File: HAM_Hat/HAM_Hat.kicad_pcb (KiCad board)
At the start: 2 copper layers, 65 x 56.5 mm, 44 parts, among them J101 TL212V-02P-G12S, J102 DB-9RS-C, J103 NCW254-02S, J104 SMA6252A2, J109 socket, J3 FHDH2.54-40, M101 Fan, Q101 BSS138, Q102 BSS138, T101 SM-LP-5001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

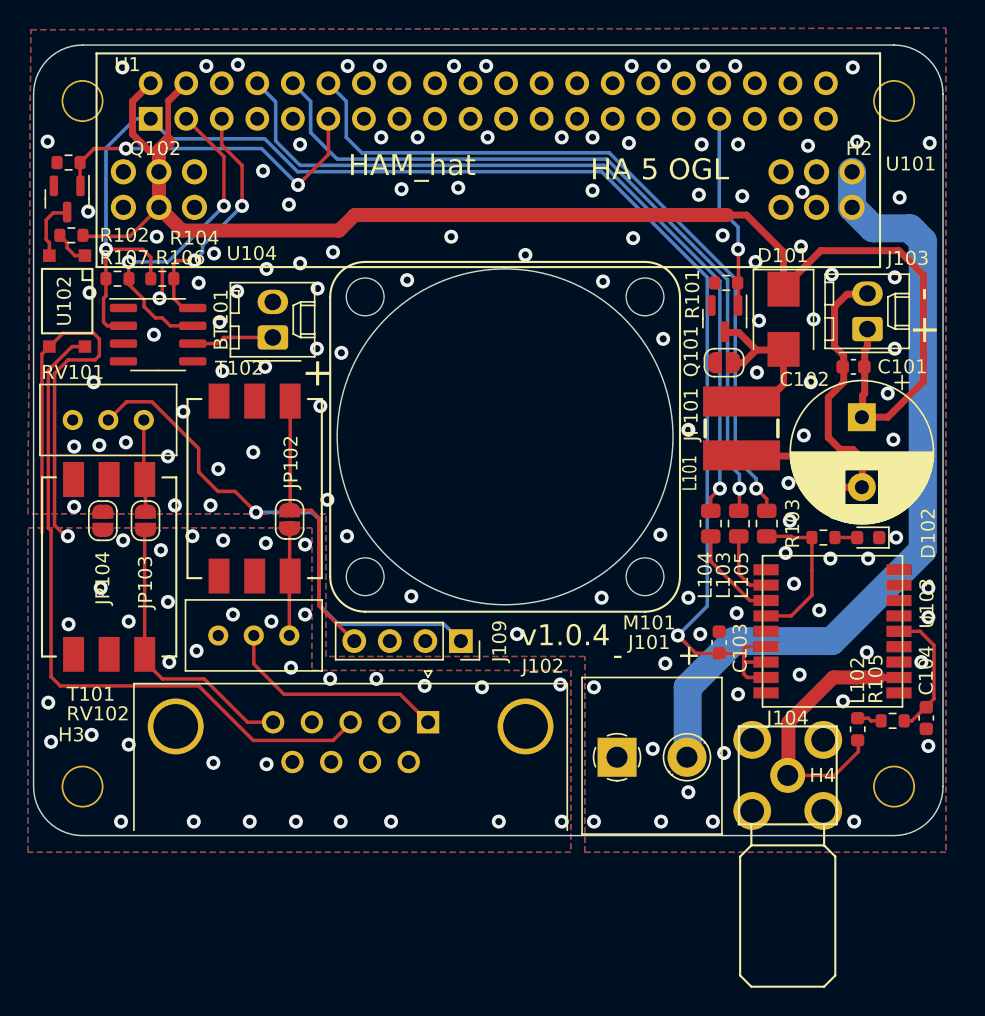
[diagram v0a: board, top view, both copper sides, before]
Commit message: Replace the DB9 connector
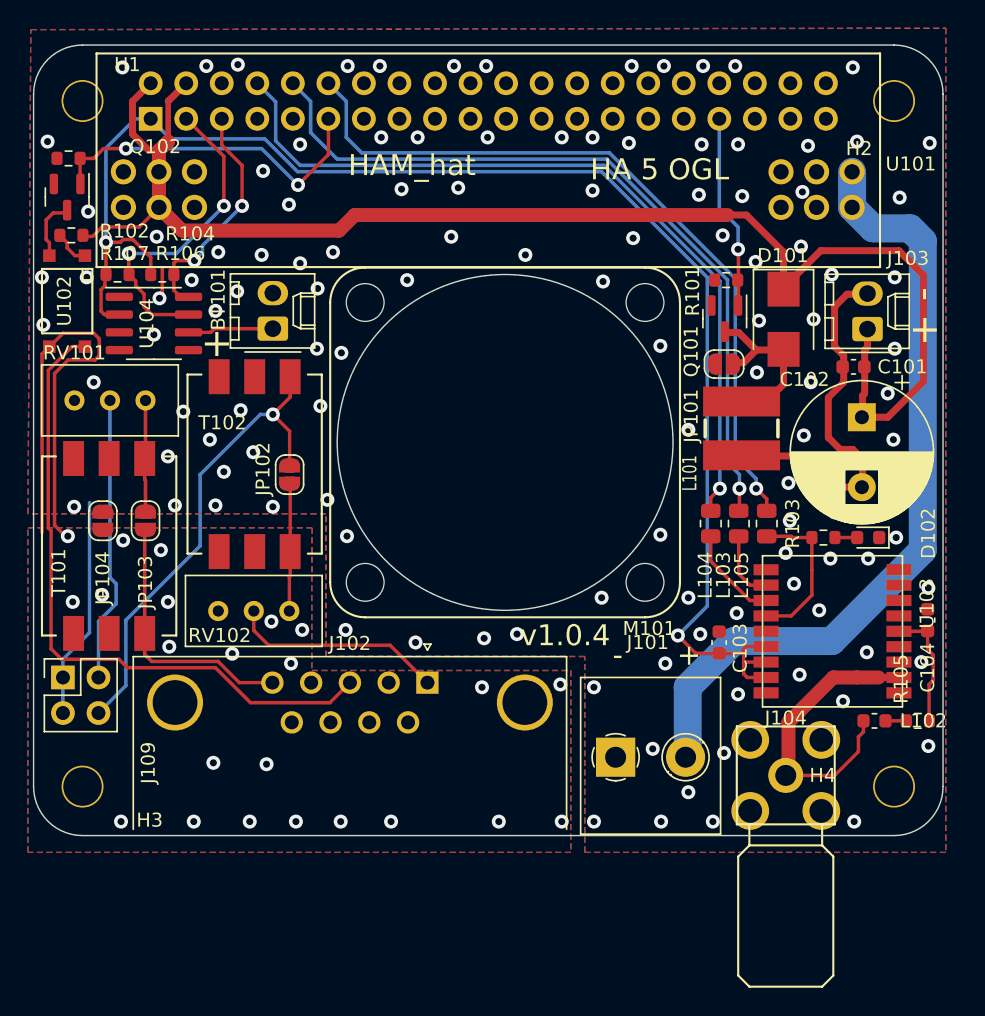
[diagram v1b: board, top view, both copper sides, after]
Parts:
- J102: footprint Connector_Dsub:DSUB-9_Female_Horizontal_P2.77x2.84mm_EdgePinOffset4.94mm_Housed_MountingHolesOffset7.48mm -> Connector_Dsub:DSUB-9_Female_Horizontal_P2.77x2.84mm_EdgePinOffset7.70mm_Housed_MountingHolesOffset9.12mm
- J109: footprint Connector_PinSocket_2.54mm:PinSocket_1x04_P2.54mm_Vertical -> Connector_PinSocket_2.54mm:PinSocket_2x02_P2.54mm_Vertical
- moved J109 28.6 mm to (118.1, 114.7), turned to 90 degrees
- moved C104 7.00 mm to (179.9, 110.6), turned to -90 degrees
- moved JP102 3.20 mm to (134.3, 100.2)
- moved J102 2.83 mm to (144.2, 115.1)
- moved R105 1.80 mm to (179.2, 117.8)
- moved RV102 1.75 mm to (129.2, 110.0)
- moved T102 1.75 mm to (131.8, 99.5)
- moved T101 1.50 mm to (121.4, 105.3)
- moved RV101 1.41 mm to (118.9, 94.9)
- moved L102 1.34 mm to (176.1, 117.8), turned to 180 degrees
- moved U104 0.85 mm to (124.6, 89.4)
- moved BT101 0.63 mm to (133.1, 89.8)
- moved M101 0.40 mm to (149.7, 97.9)
- moved R102 0.30 mm to (118.5, 77.6)
- moved R106 0.30 mm to (125.2, 85.9)
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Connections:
- J109 pad 1: Net-(J109-Pin_1) -> GND
- J109 pad 3: GND -> Net-(J109-Pin_3)
- RV101 pad 2: Net-(J109-Pin_1) -> Net-(J109-Pin_3)
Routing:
- net Net-(J109-Pin_1): track 37.4 -> 0.00 mm, vias 1 -> 0
- net Net-(J109-Pin_3): track 0.00 -> 20.5 mm
- net GND: track 2.32 -> 18.2 mm, vias 120 -> 121
- net Net-(J109-Pin_4): track 20.0 -> 34.4 mm, vias 0 -> 1
- net Net-(J102-Pad3): track 49.2 -> 46.9 mm
- net Net-(JP103-B): track 20.5 -> 18.9 mm
- net Net-(J104-In): track 19.5 -> 21.1 mm
- net Net-(JP102-B): track 7.69 -> 9.14 mm
- net Net-(JP103-A): track 6.60 -> 8.00 mm
- net Net-(J102-Pad1): track 16.2 -> 15.3 mm
- net /SCL: track 17.9 -> 17.2 mm
- net Net-(U103-VCC_RF): track 9.47 -> 8.79 mm
- net GNDA: vias 36 -> 23

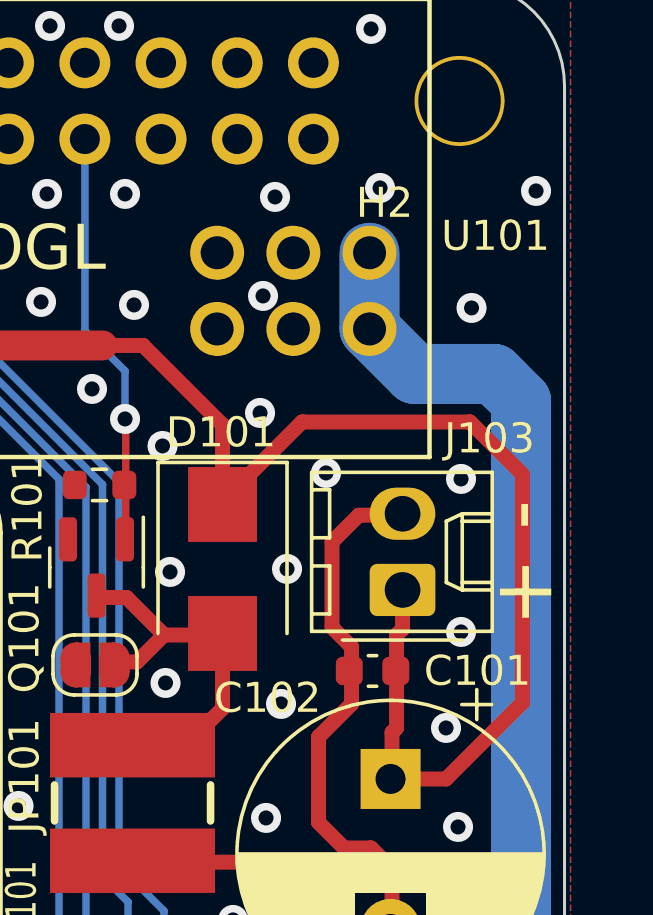
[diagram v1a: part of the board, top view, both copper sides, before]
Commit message: Add CW keying function
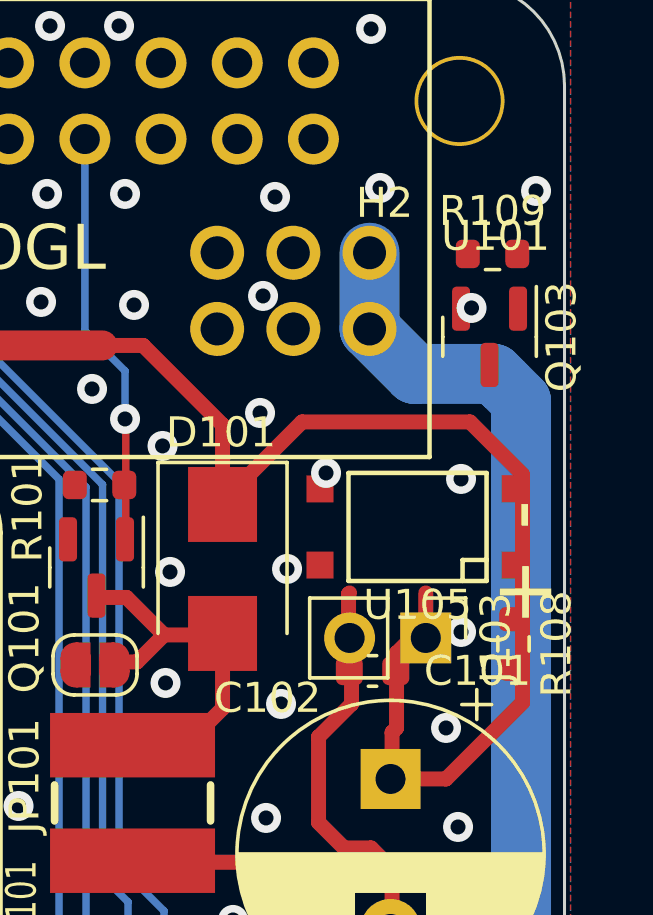
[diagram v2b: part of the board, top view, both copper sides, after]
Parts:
- added Q103: BSS138, Package_TO_SOT_SMD:SOT-23, F.Cu at (178.5, 81.4)
- added R108: 510R, Resistor_SMD:R_0603_1608Metric, F.Cu at (179.3, 91.6)
- added R109: 10k, Resistor_SMD:R_0603_1608Metric, F.Cu at (178.6, 78.6)
- added U105: TLP185, l_optocoupler:11-4M1S, F.Cu at (176.1, 87.7)
- J103: footprint Connector_Molex:Molex_KK-254_AE-6410-02A_1x02_P2.54mm_Vertical -> Connector_PinHeader_2.54mm:PinHeader_1x02_P2.54mm_Vertical
- moved J103 1.78 mm to (176.4, 91.4), turned to -90 degrees
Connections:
- J102 pad 2: unconnected-(J102-Pad2) -> Net-(J102-Pad2)
- J3 pad 40: unconnected-(J3-BCM21-Pad40) -> /CW_KEY
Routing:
- net Net-(J103-Pin_2): track 27.4 -> 22.8 mm
- net GNDA: vias 23 -> 24
- net GND: vias 121 -> 120

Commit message: Some progress on the CW keying support
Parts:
- moved R108 0.10 mm to (179.4, 91.6)
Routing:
- net Net-(J102-Pad2): track 0.00 -> 52.7 mm, vias 0 -> 2
- net GNDA: track 34.7 -> 76.2 mm, vias 24 -> 25
- net /P5V_HAT: track 103.8 -> 98.0 mm
- net Net-(Q103-D): track 0.00 -> 4.48 mm
- net Net-(R108-Pad1): track 0.00 -> 1.83 mm
- net Net-(J103-Pin_2): track 22.8 -> 21.6 mm
- net GND: vias 120 -> 118

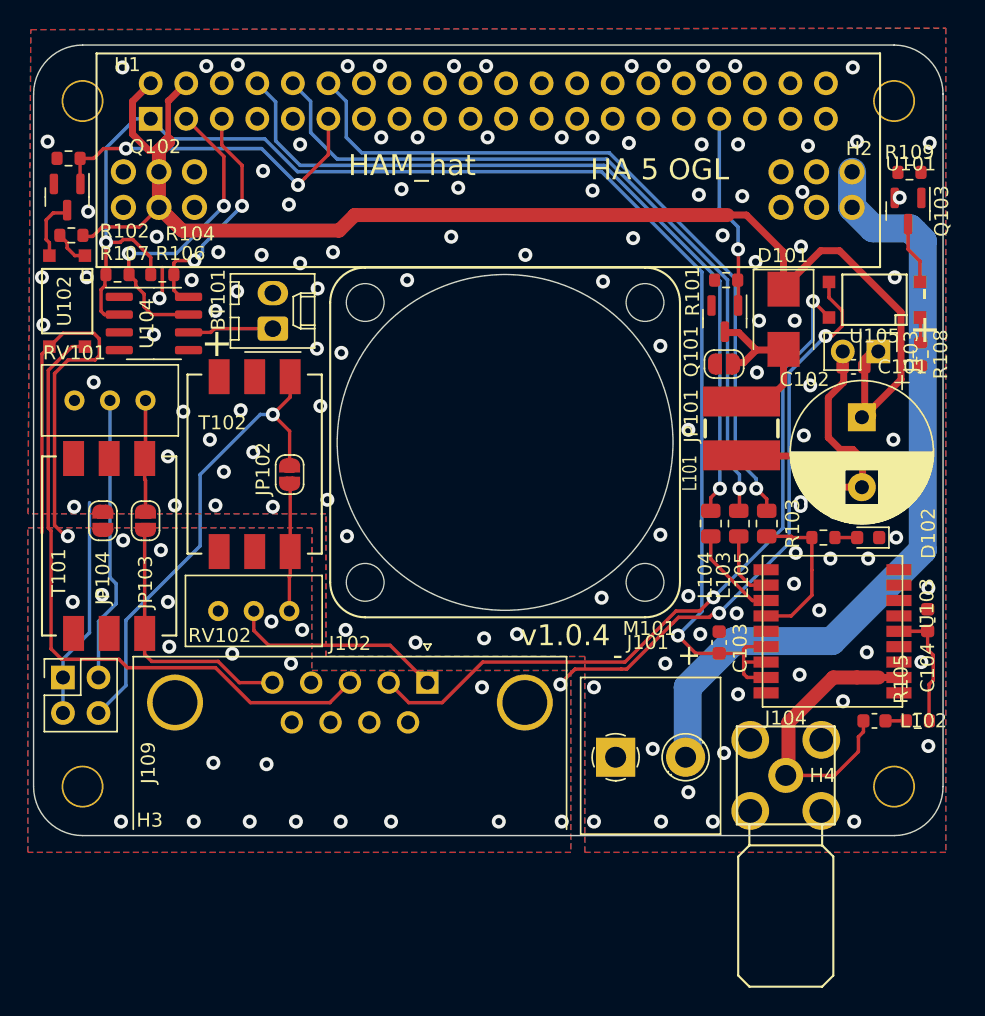
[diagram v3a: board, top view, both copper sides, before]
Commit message: CW keying added
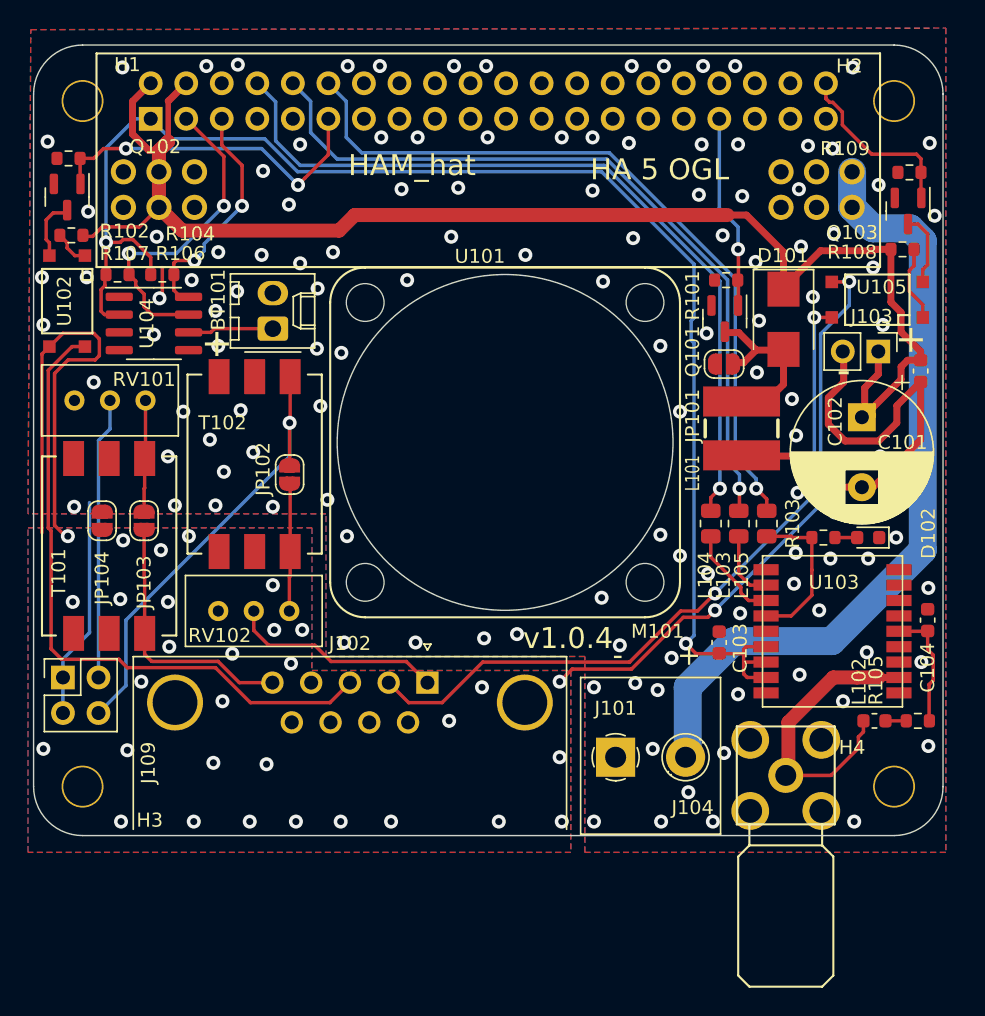
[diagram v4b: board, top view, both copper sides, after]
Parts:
- moved R108 7.61 mm to (178.1, 84.1), turned to 180 degrees
- moved C101 4.81 mm to (179.4, 92.8), turned to -90 degrees
- moved U105 0.20 mm to (176.3, 87.7)
- moved JP103 0.10 mm to (123.9, 103.5)
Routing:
- net Net-(J103-Pin_2): track 21.6 -> 34.7 mm
- net /CW_KEY: track 0.00 -> 13.0 mm
- net Net-(R108-Pad1): track 1.83 -> 5.40 mm
- net /P5V_HAT: track 98.0 -> 101.5 mm
- net Net-(J102-Pad2): track 52.7 -> 50.9 mm
- net Net-(J109-Pin_4): track 34.4 -> 32.8 mm
- net Net-(Q103-D): track 4.48 -> 5.26 mm
- net /P3V3_HAT: track 105.5 -> 104.7 mm
- net GNDA: track 76.2 -> 76.9 mm, vias 25 -> 33
- net GND: vias 118 -> 125

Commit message: Mounting holes changed
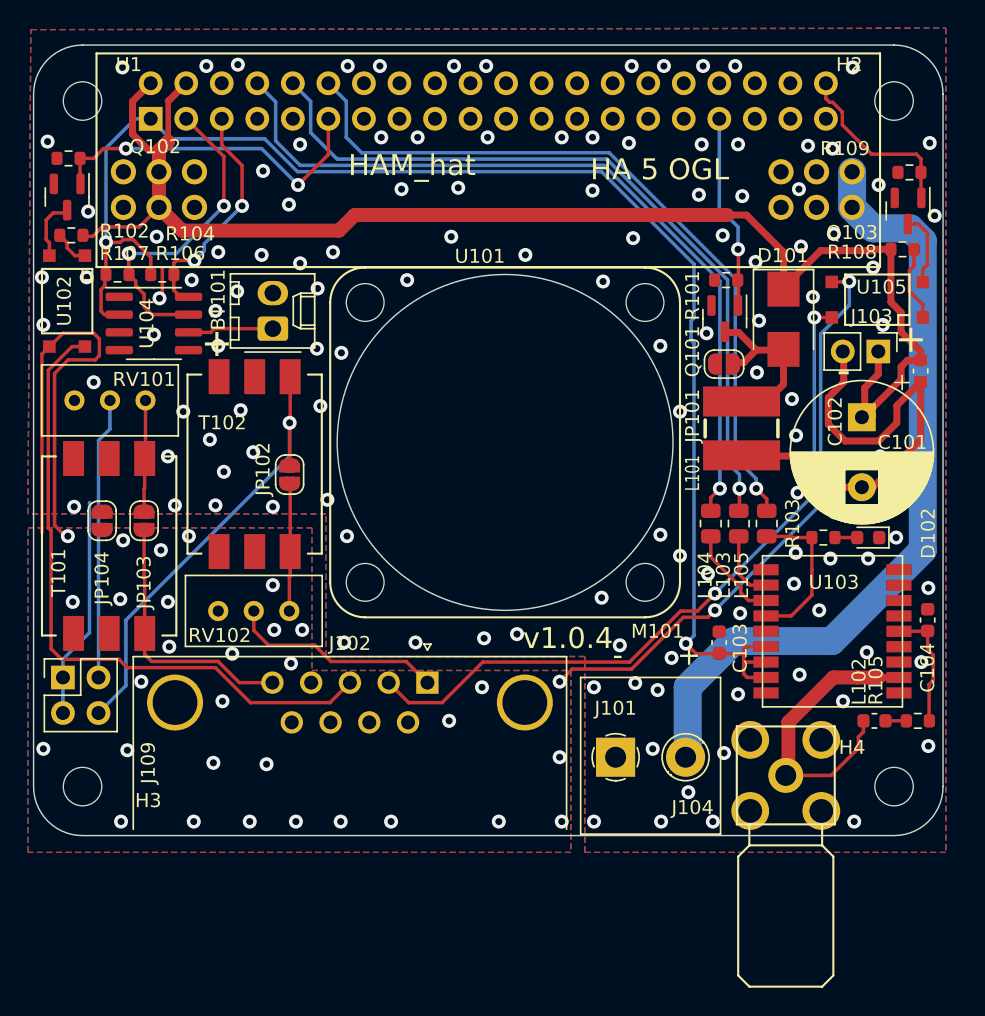
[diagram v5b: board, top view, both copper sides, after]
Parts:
- H1, H2, H3, H4: footprint project_footprints:NPTH_3mm_ID -> l_mounting_hole:l_MountingHole_Clear_2.75mm_M2.5
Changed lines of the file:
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@@
   (net 70 "Net-(Q103-D)")
   (net 71 "Net-(R108-Pad1)")
-  (footprint "project_footprints:NPTH_3mm_ID" locked (layer "F.Cu")
+  (footprint "l_mounting_hole:l_MountingHole_Clear_2.75mm_M2.5" locked (layer "F.Cu")
     (at 119.5 122.5)
     (property "Sheetfile" "HAM_Hat.kicad_sch")
@@
     (property "ki_keywords" "mounting hole")
     (attr through_hole)
-    (fp_text reference "H3" (at 4.8 2.4 180) (layer "F.SilkS")
+    (fp_text reference "H3" (at 4.7 1) (layer "F.SilkS")
         (effects (font (size 1 1) (thickness 0.15)))
     )
@@
         (effects (font (size 0.6 0.6) (thickness 0.09)))
     )
-    (pad "" np_thru_hole circle locked (at 0 0) (size 3 3) (drill 2.75) (layers "*.Cu" "*.Mask")
-      (clearance 1.6))
-  )
-  (footprint "project_footprints:NPTH_3mm_ID" locked (layer "F.Cu")
+    (pad "" np_thru_hole circle locked (at 0 0) (size 2.75 2.75) (drill 2.75) (layers "F&B.Cu" "*.Mask")
+      (solder_mask_margin 1.6) (clearance 1.6))
+  )
+  (footprint "l_mounting_hole:l_MountingHole_Clear_2.75mm_M2.5" locked (layer "F.Cu")
     (at 177.5 122.5)
     (property "Sheetfile" "HAM_Hat.kicad_sch")
@@
         (effects (font (size 0.6 0.6) (thickness 0.09)))
     )
-    (pad "" np_thru_hole circle locked (at 0 0) (size 3 3) (drill 2.75) (layers "*.Cu" "*.Mask")
-      (clearance 1.6))
+    (pad "" np_thru_hole circle locked (at 0 0) (size 2.75 2.75) (drill 2.75) (layers "F&B.Cu" "*.Mask")
+      (solder_mask_margin 1.6) (clearance 1.6))
   )
   (footprint "l_power_mod:power_mod3A" (layer "F.Cu")
@@
     )
   )
-  (footprint "project_footprints:NPTH_3mm_ID" locked (layer "F.Cu")
+  (footprint "l_mounting_hole:l_MountingHole_Clear_2.75mm_M2.5" locked (layer "F.Cu")
     (at 119.5 73.5)
     (property "Sheetfile" "HAM_Hat.kicad_sch")
@@
     (property "ki_keywords" "mounting hole")
     (attr through_hole)
-    (fp_text reference "H1" (at 3.2 -2.6) (layer "F.SilkS")
+    (fp_text reference "H1" (at 3.3 -2.6) (layer "F.SilkS")
         (effects (font (size 1 1) (thickness 0.15)))
     )
@@
         (effects (font (size 0.6 0.6) (thickness 0.09)))
     )
-    (pad "" np_thru_hole circle locked (at 0 0) (size 3 3) (drill 2.75) (layers "*.Cu" "*.Mask")
-      (clearance 1.6))
+    (pad "" np_thru_hole circle locked (at 0 0) (size 2.75 2.75) (drill 2.75) (layers "F&B.Cu" "*.Mask")
+      (solder_mask_margin 1.6) (clearance 1.6))
   )
   (footprint "Capacitor_SMD:C_0603_1608Metric" (layer "F.Cu")
@@
       ))
   )
-  (footprint "project_footprints:NPTH_3mm_ID" locked (layer "F.Cu")
+  (footprint "l_mounting_hole:l_MountingHole_Clear_2.75mm_M2.5" locked (layer "F.Cu")
     (at 177.5 73.5)
     (property "Sheetfile" "HAM_Hat.kicad_sch")
@@
     (property "ki_keywords" "mounting hole")
     (attr through_hole)
-    (fp_text reference "H2" (at -3.2 -2.5) (layer "F.SilkS")
+    (fp_text reference "H2" (at -3.2 -2.6) (layer "F.SilkS")
         (effects (font (size 1 1) (thickness 0.15)))
     )
@@
         (effects (font (size 0.6 0.6) (thickness 0.09)))
     )
-    (pad "" np_thru_hole circle locked (at 0 0) (size 3 3) (drill 2.75) (layers "*.Cu" "*.Mask")
-      (clearance 1.6))
+    (pad "" np_thru_hole circle locked (at 0 0) (size 2.75 2.75) (drill 2.75) (layers "F&B.Cu" "*.Mask")
+      (solder_mask_margin 1.6) (clearance 1.6))
   )
   (footprint "Jumper:SolderJumper-2_P1.3mm_Open_RoundedPad1.0x1.5mm" (layer "F.Cu")

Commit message: Bump version: 1.0.4 → 1.1.0
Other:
- board text added: "v1.1.0"
- board text removed: "v1.0.4"
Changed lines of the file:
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@@
     (title "Ham hat")
     (date "2021-12-03")
-    (rev "v1.0.4")
+    (rev "v1.1.0")
     (company "Logonex Bt.")
     (comment 1 "Drawn by HA5OGL")
@@
     (effects (font (size 1.5 1.5) (thickness 0.3)))
   )
-  (gr_text "v1.0.4" (at 154.2 111.9) (layer "F.SilkS")
+  (gr_text "v1.1.0" (at 154.2 111.9) (layer "F.SilkS")
     (effects (font (size 1.5 1.5) (thickness 0.3)))
   )

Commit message: Connect more GND to the connector
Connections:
- J102 pad 7: unconnected-(J102-Pad7) -> GNDA
- J102 pad 8: unconnected-(J102-Pad8) -> GNDA
- J102 pad 9: unconnected-(J102-Pad9) -> GNDA
